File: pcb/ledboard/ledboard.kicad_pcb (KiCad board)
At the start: 2 copper layers, 74 x 27.5 mm, 38 parts, among them J1 LEFT, J2 PWR_L, J3 RIGHT, J4 PWR_R, U1 AL8860, U2 AL8860

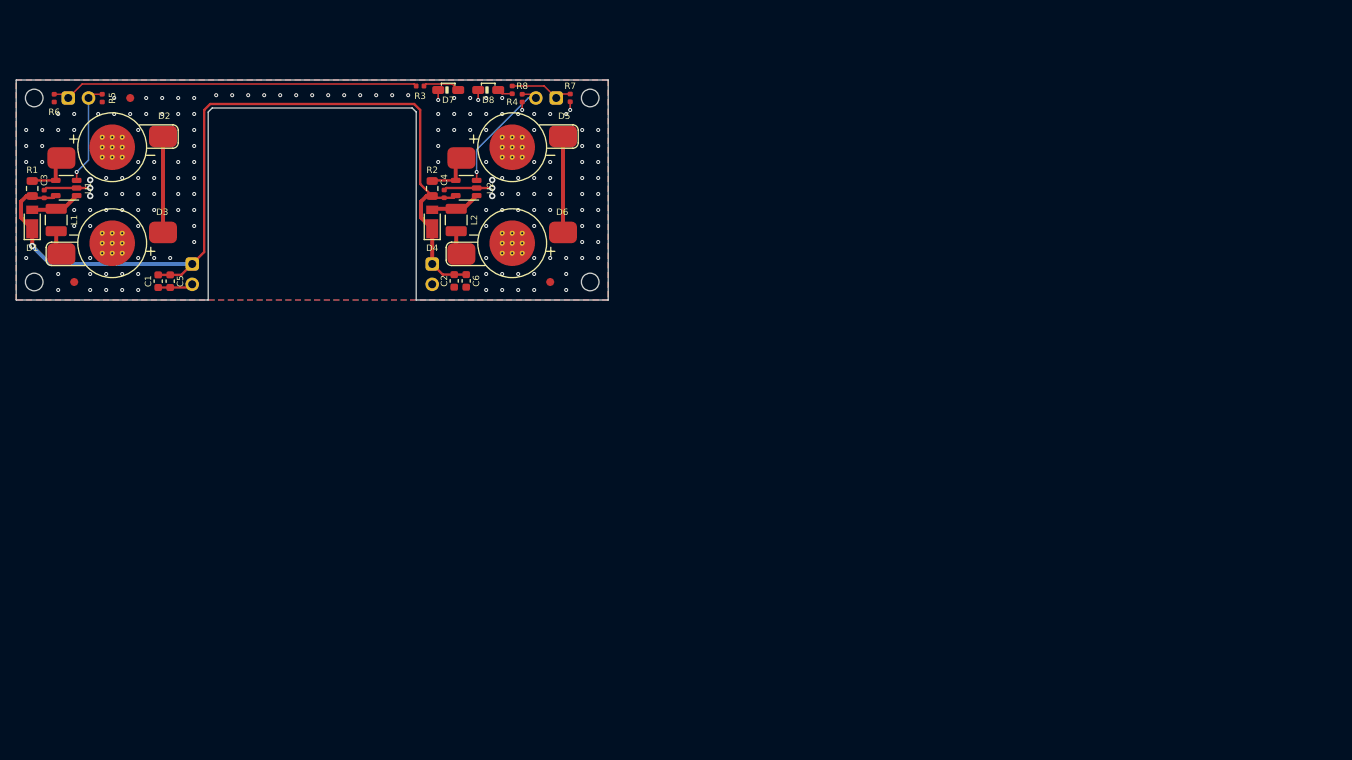
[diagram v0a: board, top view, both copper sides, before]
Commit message: Created LED Board
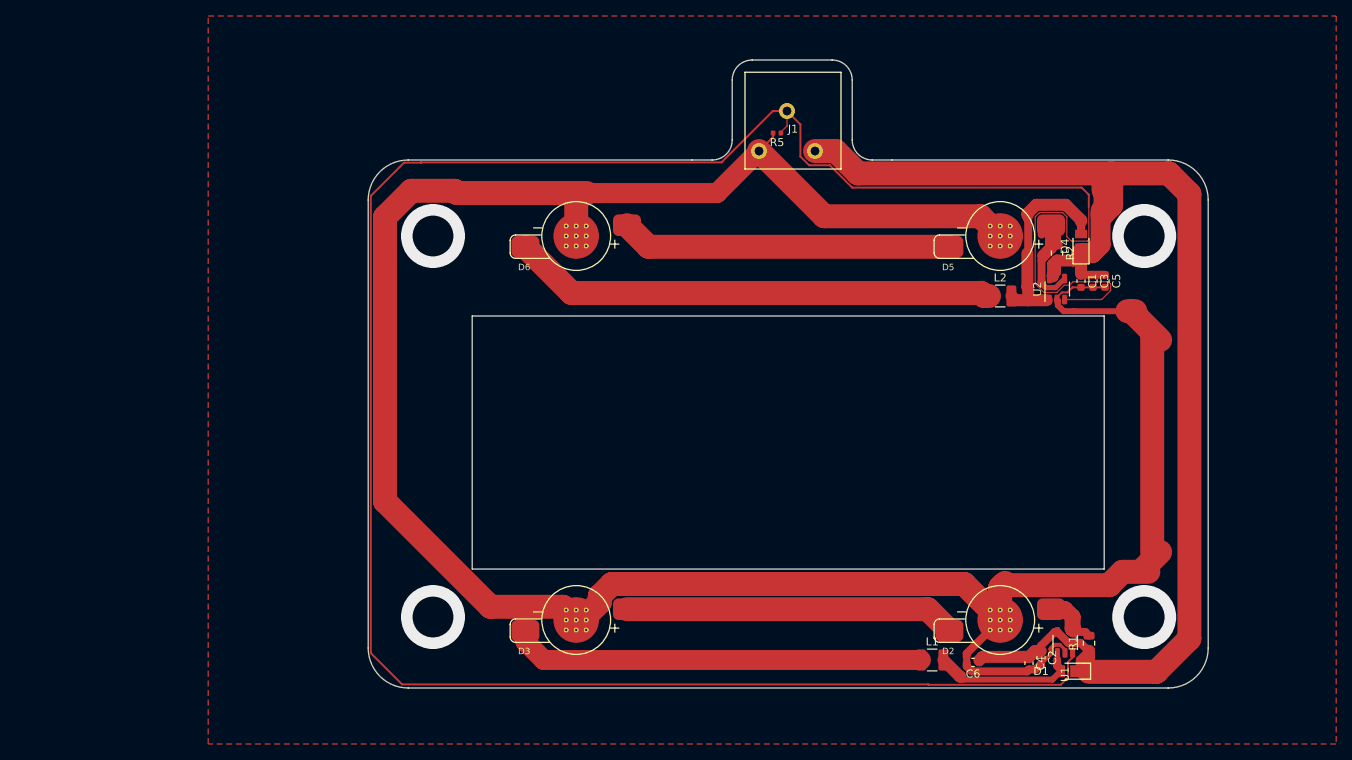
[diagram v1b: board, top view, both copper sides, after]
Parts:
- removed D7: GRN, ledboard:LTST-S220
- removed D8: RED, ledboard:LTST-S220
- removed FID1, FID2, FID3: Fiducial_1mm_Mask2mm, Fiducial:Fiducial_1mm_Mask2mm
- removed J2: PWR_L, ledboard:PinHeader_1x02_P2.54mm_Vertical_RoundRect
- removed J3: RIGHT, ledboard:PinHeader_1x02_P2.54mm_Vertical_RoundRect
- removed J4: PWR_R, ledboard:PinHeader_1x02_P2.54mm_Vertical_RoundRect
- removed R3, R4: 180, Resistor_SMD:R_0402_1005Metric
- removed R6, R7, R8: 47k, Resistor_SMD:R_0402_1005Metric
- removed REF** (x4): MountingHole_2.2mm_M2_ISO7380, MountingHole:MountingHole_2.2mm_M2_ISO7380
- removed REF**: OSHW-Symbol_22.3x20mm_SilkScreen, Symbol:OSHW-Symbol_22.3x20mm_SilkScreen
- C3, C4: footprint Capacitor_SMD:C_0402_1005Metric -> Capacitor_SMD:C_0603_1608Metric
- J1: value LEFT -> Conn_01x03; footprint ledboard:PinHeader_1x02_P2.54mm_Vertical_RoundRect -> ledboard:WJ250B-3pin; moved to F.Cu
- moved R1 143.8 mm to (167.1, 110.4)
- moved D1 141.7 mm to (165.1, 113.9), turned to 180 degrees
- moved U1 137.2 mm to (164.1, 110.3), turned to 90 degrees
- moved C3 131.6 mm to (167.6, 65.1), turned to 270 degrees
- moved D2 125.8 mm to (156.0, 107.5), turned to 0 degrees
- moved L1 122.5 mm to (147.5, 112.5), turned to 0 degrees
- moved C5 116.9 mm to (169.1, 65.1)
- moved C1 115.4 mm to (166.1, 65.1)
- moved J1 97.0 mm to (136.1, 51.1), turned to 180 degrees
- moved C4 93.7 mm to (159.6, 112.9), turned to 270 degrees
- moved C2 87.2 mm to (161.1, 112.2)
- moved R5 84.5 mm to (128.1, 46.6), turned to 180 degrees
- moved D4 81.2 mm to (166.1, 60.8)
- moved C6 79.3 mm to (152.6, 112.8), turned to 180 degrees
- moved R2 78.5 mm to (163.1, 61.6)
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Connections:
- J1 pad 1: /USR_LED_A -> +12V
- J1 pad 2: /CTRL_L -> /CTRL
- R5 pad 1: /CTRL_L -> /CTRL
- U1 pad 3: /CTRL_L -> /CTRL
- U2 pad 3: /CTRL_R -> /CTRL
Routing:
- net /CTRL: track 0.00 -> 295.0 mm
- net GND: track 20.9 -> 315.7 mm, vias 162 -> 0
- net +12V: track 113.6 -> 186.5 mm, vias 1 -> 0
- net Net-(D6-Pad1): track 3.12 -> 60.5 mm
- net Net-(D3-Pad1): track 3.12 -> 51.8 mm
- net /USR_LED_A: track 46.3 -> 0.00 mm
- net Net-(D5-Pad1): track 12.0 -> 41.4 mm
- net Net-(D2-Pad1): track 12.0 -> 41.4 mm
- net Net-(D4-Pad2): track 6.30 -> 25.6 mm
- net /CTRL_R: track 15.8 -> 0.00 mm, vias 1 -> 0
- net Net-(D1-Pad2): track 6.30 -> 21.6 mm
- net /CTRL_L: track 12.8 -> 0.00 mm, vias 1 -> 0
- net Net-(D5-Pad2): track 6.07 -> 17.0 mm
- net /USR_LED_B: track 8.08 -> 0.00 mm
- net Net-(D7-Pad2): track 4.69 -> 0.00 mm
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- removed copper zone on B.Cu, net GND
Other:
- board size 74 x 27.5 mm -> 105 x 78.5 mm
- rule trace_min: 0.15 -> 0.127
- board text removed: "Camera is 25mm wide, 24mm tall."
- board text removed: "LED Board"
- board text removed: "Licensed under CERN-OHL-P v2"
- board text removed: "rev v0.4.2"
- board text removed: "© Franklin Harding 2020"

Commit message: Finished pcb
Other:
- outline, holes or cut-outs redrawn
- board text added: "LED Booster By Ethan Cao Rev. 1"
